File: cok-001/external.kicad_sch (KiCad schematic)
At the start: 42 parts, among them J3208 凸, J3209 ATA Power, J3221 ATA0 for BD

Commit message: update to 9
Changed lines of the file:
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@@
 (kicad_sch
-	(version 20231120)
+	(version 20250114)
 	(generator "eeschema")
-	(generator_version "8.0")
+	(generator_version "9.0")
 	(paper "A4")
 	(junction

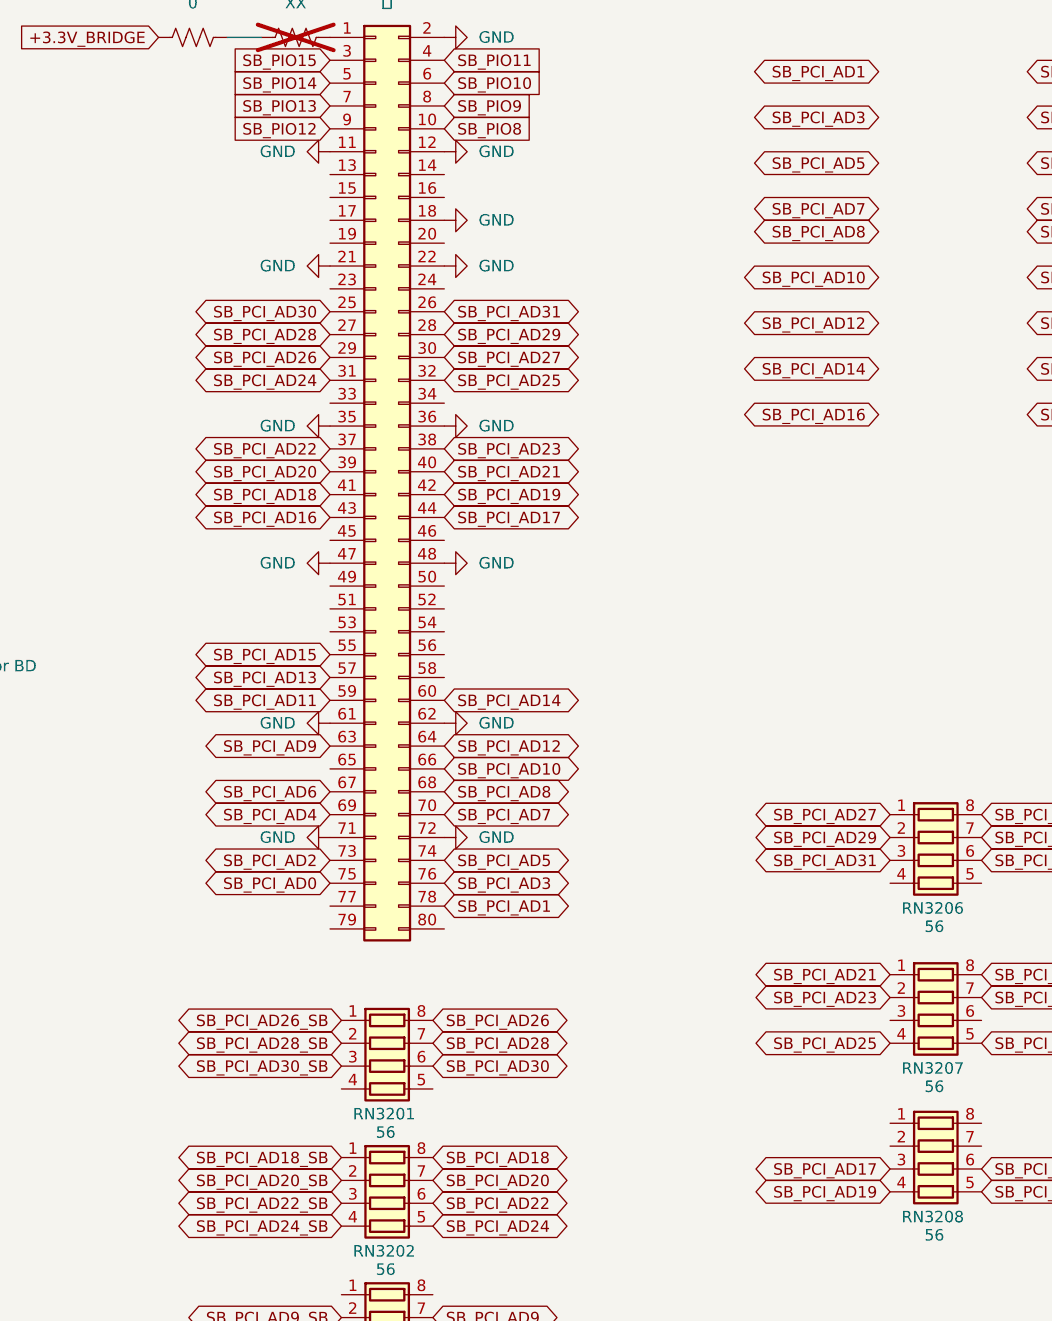
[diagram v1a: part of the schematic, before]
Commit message: more pci pins
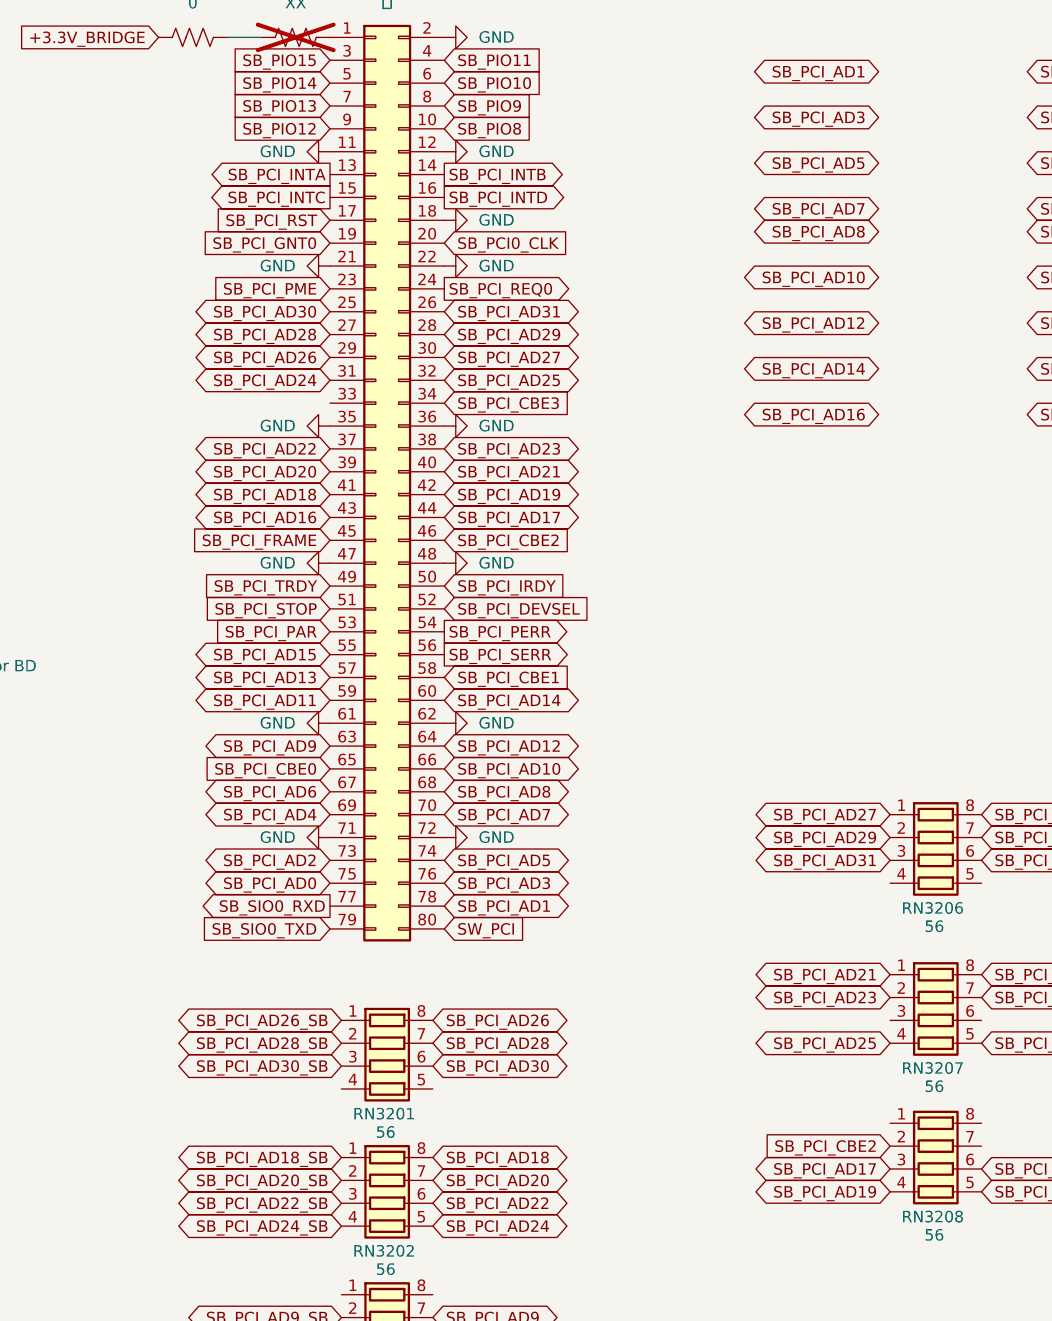
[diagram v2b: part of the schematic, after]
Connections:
- net SB_PCI_CBE2: now reaches RN3208.2 (R2.1)
- net SB_PCI_CBE2: now also J3208.46 (Pin_46)
- net SB_PCI_INTA: now reaches J3208.13 (Pin_13)
- net SB_PCI_INTB: now reaches J3208.14 (Pin_14)
- net SB_PCI_INTC: now reaches J3208.15 (Pin_15)
- net SB_PCI_INTD: now reaches J3208.16 (Pin_16)
- net SB_PCI_RST: now reaches J3208.17 (Pin_17)
- net SB_PCI_GNT0: now reaches J3208.19 (Pin_19)
- net SB_PCI0_CLK: now reaches J3208.20 (Pin_20)
- net SB_PCI_PME: now reaches J3208.23 (Pin_23)
- net SB_PCI_REQ0: now reaches J3208.24 (Pin_24)
- net SB_PCI_CBE3: now reaches J3208.34 (Pin_34)
- net SB_PCI_FRAME: now reaches J3208.45 (Pin_45)
- net SB_PCI_TRDY: now reaches J3208.49 (Pin_49)
- net SB_PCI_IRDY: now reaches J3208.50 (Pin_50)
- net SB_PCI_STOP: now reaches J3208.51 (Pin_51)
- net SB_PCI_DEVSEL: now reaches J3208.52 (Pin_52)
- net SB_PCI_PAR: now reaches J3208.53 (Pin_53)
- net SB_PCI_PERR: now reaches J3208.54 (Pin_54)
- net SB_PCI_SERR: now reaches J3208.56 (Pin_56)
- net SB_PCI_CBE1: now reaches J3208.58 (Pin_58)
- net SB_PCI_CBE0: now reaches J3208.65 (Pin_65)
- net SB_SIO0_RXD: now reaches J3208.77 (Pin_77)
- net SB_SIO0_TXD: now reaches J3208.79 (Pin_79)
- net SW_PCI: now reaches J3208.80 (Pin_80)

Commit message: pci
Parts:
- added Q3201: DTC144E, Package_TO_SOT_SMD:SOT-323_SC-70, symbol Transistor_BJT:DTC144E
- added R3228: 82, Resistor_SMD:R_0402_1005Metric, symbol Device:R_US
- added R3229, R3230, R3232: 22, Resistor_SMD:R_0402_1005Metric, symbol Device:R_US
- added R3231, R3282, R3283, R3284, R3285, R3286, R3287, R3298: 0, Resistor_SMD:R_0402_1005Metric, symbol Device:R_US
- added R3233, R3234, R3236, R3237, R3238, R3239: 33, Resistor_SMD:R_0402_1005Metric, symbol Device:R_US
- added RN3209, RN3210, RN3211: 56, Resistor_SMD:R_Array_Convex_4x0402, symbol Device:R_Pack04
- added TP3222: TestPoint, TestPoint:TestPoint_Pad_1.0x1.0mm, symbol Connector:TestPoint
- J3209: footprint Connector_JST:JST_PH_B4B-PH-SM4-TB_1x04-1MP_P2.00mm_Vertical -> Connector_JST:JST_PH_S4B-PH-SM4-TB_1x04-1MP_P2.00mm_Horizontal; symbol Connector:Conn_01x04_Socket -> Connector_Generic_MountingPin:Conn_01x04_MountingPin
- J3221: value ATA0 for BD -> IMSA-9637S-60Y801
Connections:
- net SB_PCI_CBE0 is gone; now on net ~{SB_PCI_CBE0}: J3208.65 (Pin_65)
- net SB_PCI_CBE3 is gone; now on net ~{SB_PCI_CBE3}: J3208.34 (Pin_34)
- net SB_PCI_IRDY is gone; now on net ~{SB_PCI_IRDY}: J3208.50 (Pin_50)
- net SB_PCI_RST is gone; now on net ~{SB_PCI_RST}: J3208.17 (Pin_17)
- net SB_PCI_STOP is gone; now on net ~{SB_PCI_STOP}: J3208.51 (Pin_51)
- net SB_PCI_TRDY is gone; now on net ~{SB_PCI_TRDY}: J3208.49 (Pin_49)
- net GND: now also J3209.MP (MountPin), Q3201.2 (E)
- net SB_PCI_AD1: now also RN3209.2 (R2.1)
- net SB_PCI_AD10: now also RN3211.3 (R3.1)
- net SB_PCI_AD10_SB: now also RN3211.6 (R3.2)
- net SB_PCI_AD12: now also RN3211.4 (R4.1)
- net SB_PCI_AD12_SB: now also RN3211.5 (R4.2)
- net SB_PCI_AD14: now also RN3210.1 (R1.1)
- net SB_PCI_AD14_SB: now also RN3210.8 (R1.2)
- net SB_PCI_AD1_SB: now also RN3209.7 (R2.2)
- net SB_PCI_AD3: now also RN3209.3 (R3.1)
- net SB_PCI_AD3_SB: now also RN3209.6 (R3.2)
- net SB_PCI_AD5: now also RN3209.4 (R4.1)
- net SB_PCI_AD5_SB: now also RN3209.5 (R4.2)
- net SB_PCI_AD7: now also RN3211.1 (R1.1)
- net SB_PCI_AD7_SB: now also RN3211.8 (R1.2)
- net SB_PCI_AD8: now also RN3211.2 (R2.1)
- net SB_PCI_AD8_SB: now also RN3211.7 (R2.2)
- net SB_PCI_PAR: now also RN3205.7 (R2.2)
- net ~{SB_PCI_IRDY}: now reaches RN3208.1 (R1.1)
- net ~{SB_PCI_CBE2_SB}: now reaches RN3208.7 (R2.2)
- net ~{SB_PCI_IRDY_SB}: now reaches RN3208.8 (R1.2)
- net ~{SB_PCI_CBE3}: now reaches RN3207.3 (R3.1)
- net ~{SB_PCI_CBE3_SB}: now reaches RN3207.6 (R3.2)
- net at J3221.20 (Pin_20): now also R3232.2
- net at J3221.22 (Pin_22): now also R3231.2
- net at J3221.24 (Pin_24): now also R3230.2
- net at J3221.26 (Pin_26): now also R3229.2
- net at J3221.28 (Pin_28): now also R3228.2
- net SB_ATA0_DASP: now reaches J3221.30 (Pin_30)
- net at J3221.31 (Pin_31): now also R3239.2
- net at J3221.32 (Pin_32): now also R3238.2
- net at J3221.33 (Pin_33): now also R3237.2
- net at J3221.34 (Pin_34): now also R3236.2
- net at J3221.36 (Pin_36): now also R3234.2
- net at J3221.37 (Pin_37): now also R3233.2
- net XSB_CBLID: now reaches J3221.43 (Pin_43)
- net XSB_CBLID: now also Q3201.1 (B)
- net at J3221.44 (Pin_44): now also TP3222.1
- net at J3221.46 (Pin_46): now also R3283.2
- net at J3221.47 (Pin_47): now also R3282.2
- net MC_P_OFF_REQ: now reaches J3221.48 (Pin_48)
- net MC_RESERVED: now reaches J3221.49 (Pin_49)
- net BD_LED: now reaches J3221.50 (Pin_50)
- net at J3221.52 (Pin_52): now also R3287.2
- net PHOTO_LED: now reaches J3221.53 (Pin_53)
- net at J3221.54 (Pin_54): now also R3286.2
- net DISC_IN_MECHA: now reaches J3221.55 (Pin_55)
- net EJECT_MECHA: now reaches J3221.56 (Pin_56)
- net at J3221.57 (Pin_57): now also R3285.2
- net at J3221.58 (Pin_58): now also R3284.2
- net ~{SB_PCI_GNT1}: now reaches RN3206.4 (R4.1)
- net ~{SB_PCI_GNT1_SB}: now reaches RN3206.5 (R4.2)
- net SB_PCI_PAR_SB: now reaches RN3205.2 (R2.1)
- net ~{SB_PCI_STOP_SB}: now reaches RN3205.3 (R3.1)
- net ~{SB_PCI_TRDY_SB}: now reaches RN3205.4 (R4.1)
- net ~{SB_PCI_TRDY}: now reaches RN3205.5 (R4.2)
- net ~{SB_PCI_STOP}: now reaches RN3205.6 (R3.2)
- net ~{SB_PCI_CBE0_SB}: now reaches RN3203.1 (R1.1)
- net ~{SB_PCI_CBE0}: now reaches RN3203.8 (R1.2)
- net ~{SB_PCI_RST_SB}: now reaches RN3201.4 (R4.1)
- net ~{SB_PCI_RST}: now reaches RN3201.5 (R4.2)
- net SB_PCI_CBE1 renamed ~{SB_PCI_CBE1}
- net ~{SB_PCI_CBE1}: now also RN3209.1 (R1.1)
- net SB_PCI_CBE2 renamed ~{SB_PCI_CBE2}
- net SB_PCI_DEVSEL renamed ~{SB_PCI_DEVSEL}
- net ~{SB_PCI_DEVSEL}: now also RN3210.4 (R4.1)
- net SB_PCI_FRAME renamed ~{SB_PCI_FRAME}
- net SB_PCI_GNT0 renamed ~{SB_PCI_GNT0}
- net SB_PCI_INTA renamed ~{SB_PCI_INTA}
- net SB_PCI_INTB renamed ~{SB_PCI_INTB}
- net SB_PCI_INTC renamed ~{SB_PCI_INTC}
- net SB_PCI_INTD renamed ~{SB_PCI_INTD}
- net SB_PCI_PERR renamed ~{SB_PCI_PERR}
- net ~{SB_PCI_PERR}: now also RN3210.3 (R3.1)
- net SB_PCI_PME renamed ~{SB_PCI_PME}
- net SB_PCI_REQ0 renamed ~{SB_PCI_REQ0}
- net SB_PCI_SERR renamed ~{SB_PCI_SERR}
- net ~{SB_PCI_SERR}: now also RN3210.2 (R2.1)
- new net DISC_CHUCK: R3286.1
- new net DISC_IN: R3287.1
- new net DISC_OUT12_SW: R3284.1
- new net DISC_OUT8_SW: R3285.1
- new net MC_ALIVE: R3282.1
- new net MECHA_INT: R3283.1
- new net SB_ATA0_CS0: R3238.1
- new net SB_ATA0_CS1: R3239.1
- new net SB_ATA0_DA0: R3236.1
- new net SB_ATA0_DA1: R3234.1
- new net SB_ATA0_DA2: R3237.1
- new net SB_ATA0_DIOR: R3230.1
- new net SB_ATA0_DIOW: R3229.1
- new net SB_ATA0_DMACK: R3232.1
- new net SB_ATA0_DMARQ: R3228.1
- new net SB_ATA0_INTRQ: R3233.1
- new net SB_ATA0_IORDY: R3231.1
- new net SB_ATA0_PDIAG: Q3201.3 (C)
- new net ~{SB_PCI_CBE1_SB}: RN3209.8 (R1.2)
- new net ~{SB_PCI_DEVSEL_SB}: RN3210.5 (R4.2)
- new net ~{SB_PCI_PERR_SB}: RN3210.6 (R3.2)
- new net ~{SB_PCI_SERR_SB}: RN3210.7 (R2.2)
- no-connect marks 0 -> 5

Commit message: cr
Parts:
- added J3219: for Multi_Card_Board, Connector_FFC-FPC:Hirose_FH12-15S-0.5SH_1x15-1MP_P0.50mm_Horizontal, symbol Connector_Generic_MountingPin:Conn_01x15_MountingPin
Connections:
- net GND: now also J3219.1 (Pin_1), J3219.13 (Pin_13), J3219.15 (Pin_15), J3219.2 (Pin_2), J3219.5 (Pin_5), J3219.6 (Pin_6), J3219.8 (Pin_8), J3219.MP (MountPin)
